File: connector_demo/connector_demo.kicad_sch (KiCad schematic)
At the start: 3 parts, among them J1 PicoBlade 8-wide, J2 PicoLock 8-wide, J3 MicroLock

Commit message: added connector names
still confirming pin 1
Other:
- company: (none) -> CalgaryToSpace
- title: (none) -> Connector PCB
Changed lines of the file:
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@@
 	(generator "eeschema")
 	(generator_version "9.0")
-	(paper "A4")
+	(paper "A")
+	(title_block
+		(title "Connector PCB")
+		(date "2025-03-28")
+		(rev "1")
+		(company "CalgaryToSpace")
+	)
 	(symbol
 		(lib_id "Connector_Generic:Conn_01x08")

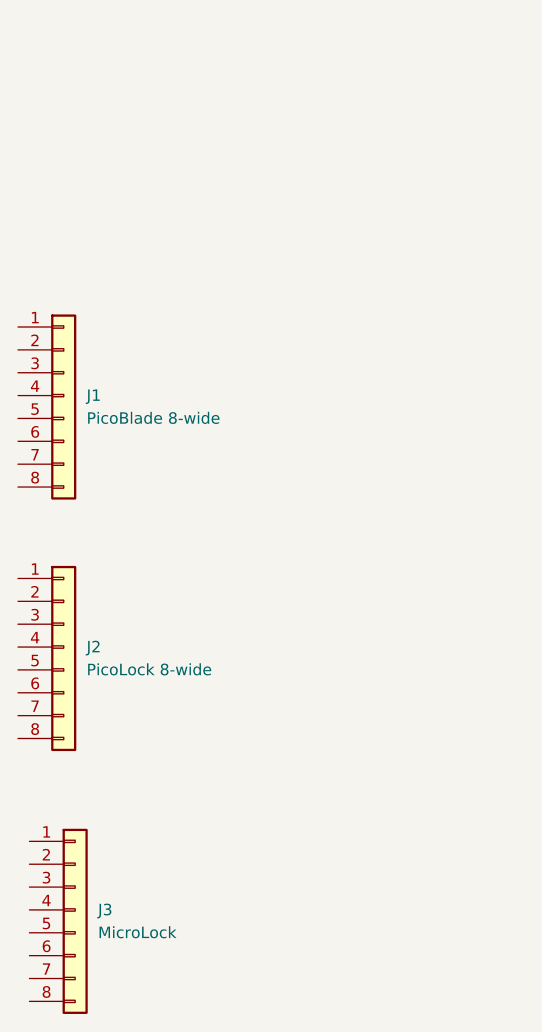
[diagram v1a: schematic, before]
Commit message: added header pins and traces
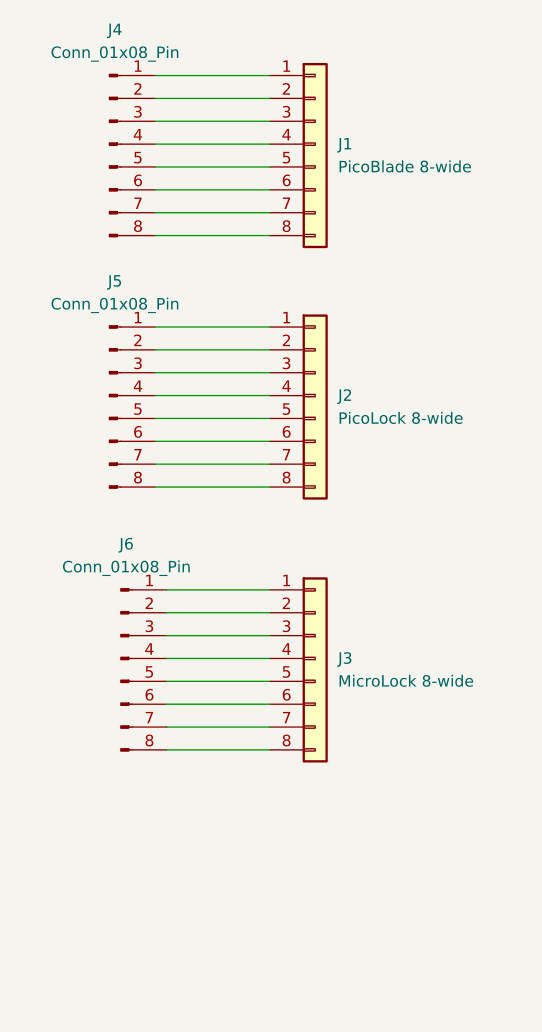
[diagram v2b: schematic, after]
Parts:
- added J4, J5, J6: Conn_01x08_Pin, Connector_PinHeader_2.54mm:PinHeader_1x08_P2.54mm_Vertical, symbol Connector:Conn_01x08_Pin
- J3: value MicroLock -> MicroLock 8-wide
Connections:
- net at J3.1 (Pin_1): now also J6.1 (Pin_1)
- net at J3.2 (Pin_2): now also J6.2 (Pin_2)
- net at J3.3 (Pin_3): now also J6.3 (Pin_3)
- net at J3.4 (Pin_4): now also J6.4 (Pin_4)
- net at J3.5 (Pin_5): now also J6.5 (Pin_5)
- net at J3.6 (Pin_6): now also J6.6 (Pin_6)
- net at J3.7 (Pin_7): now also J6.7 (Pin_7)
- net at J3.8 (Pin_8): now also J6.8 (Pin_8)
- net at J2.1 (Pin_1): now also J5.1 (Pin_1)
- net at J2.2 (Pin_2): now also J5.2 (Pin_2)
- net at J2.3 (Pin_3): now also J5.3 (Pin_3)
- net at J2.4 (Pin_4): now also J5.4 (Pin_4)
- net at J2.5 (Pin_5): now also J5.5 (Pin_5)
- net at J2.6 (Pin_6): now also J5.6 (Pin_6)
- net at J2.7 (Pin_7): now also J5.7 (Pin_7)
- net at J2.8 (Pin_8): now also J5.8 (Pin_8)
- net at J1.1 (Pin_1): now also J4.1 (Pin_1)
- net at J1.2 (Pin_2): now also J4.2 (Pin_2)
- net at J1.3 (Pin_3): now also J4.3 (Pin_3)
- net at J1.4 (Pin_4): now also J4.4 (Pin_4)
- net at J1.5 (Pin_5): now also J4.5 (Pin_5)
- net at J1.6 (Pin_6): now also J4.6 (Pin_6)
- net at J1.7 (Pin_7): now also J4.7 (Pin_7)
- net at J1.8 (Pin_8): now also J4.8 (Pin_8)
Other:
- moved on the sheet: J1, J2, J3

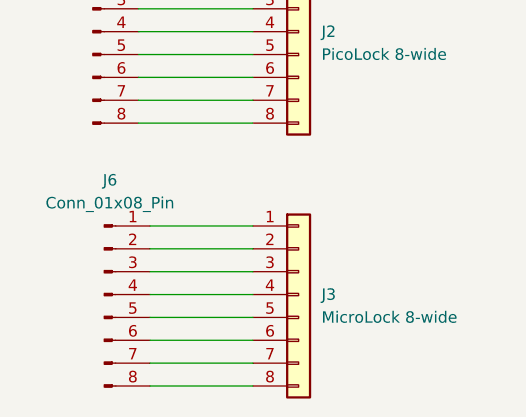
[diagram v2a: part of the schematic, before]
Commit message: Fixed microlock connector, generated BOM
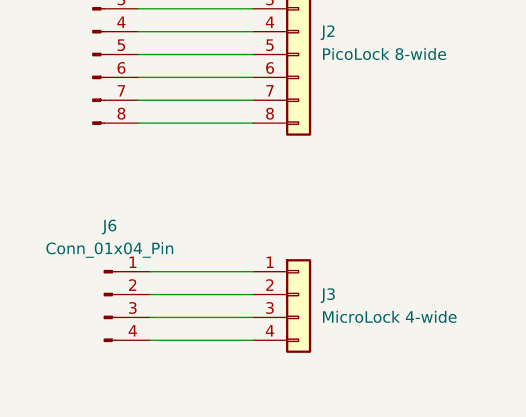
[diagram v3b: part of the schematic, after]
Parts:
- J3: value MicroLock 8-wide -> MicroLock 4-wide; footprint Connector_Molex:Molex_Pico-Lock_504050-0891_1x08-1MP_P1.50mm_Horizontal -> microlock:CONN04_5055670471_MOL; symbol Connector_Generic:Conn_01x08 -> Connector_Generic:Conn_01x04
- J6: value Conn_01x08_Pin -> Conn_01x04_Pin; footprint Connector_PinHeader_2.54mm:PinHeader_1x08_P2.54mm_Vertical -> Connector_PinHeader_2.54mm:PinHeader_1x04_P2.54mm_Vertical; symbol Connector:Conn_01x08_Pin -> Connector:Conn_01x04_Pin
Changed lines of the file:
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@@
-	(wire
-		(pts
-			(xy 87.63 111.76) (xy 99.06 111.76)
-		)
-		(stroke
-			(width 0)
-			(type default)
-		)
-	)
 	(wire
 		(pts
@@
 	(wire
 		(pts
-			(xy 87.63 99.06) (xy 99.06 99.06)
-		)
-		(stroke
-			(width 0)
-			(type default)
-		)
-	)
-	(wire
-		(pts
 			(xy 87.63 101.6) (xy 99.06 101.6)
 		)
@@
 	(wire
 		(pts
-			(xy 87.63 96.52) (xy 99.06 96.52)
-		)
-		(stroke
-			(width 0)
-			(type default)
-		)
-	)
-	(wire
-		(pts
 			(xy 86.36 46.99) (xy 99.06 46.99)
 		)
@@
 		(pts
 			(xy 86.36 82.55) (xy 99.06 82.55)
-		)
-		(stroke
-			(width 0)
-			(type default)
-		)
-	)
-	(wire
-		(pts
-			(xy 87.63 114.3) (xy 99.06 114.3)
 		)
 		(stroke
@@
 	)
 	(symbol
-		(lib_id "Connector_Generic:Conn_01x08")
+		(lib_id "Connector_Generic:Conn_01x04")
 		(at 104.14 104.14 0)
 		(unit 1)
@@
 			)
 		)
-		(property "Value" "MicroLock 8-wide"
+		(property "Value" "MicroLock 4-wide"
 			(at 106.68 106.6799 0)
 			(effects
@@
 			)
 		)
-		(property "Footprint" "Connector_Molex:Molex_Pico-Lock_504050-0891_1x08-1MP_P1.50mm_Horizontal"
+		(property "Footprint" "microlock:CONN04_5055670471_MOL"
 			(at 104.14 104.14 0)
 			(effects
@@
 			)
 		)
-		(property "Description" "Generic connector, single row, 01x08, script generated (kicad-library-utils/schlib/autogen/connector/)"
+		(property "Description" "Generic connector, single row, 01x04, script generated (kicad-library-utils/schlib/autogen/connector/)"
 			(at 104.14 104.14 0)
 			(effects
@@
 			)
 		)
-		(pin "6"
-		)
 		(pin "2"
 		)
-		(pin "5"
-		)
 		(pin "4"
 		)
@@
 		)
 		(pin "3"
-		)
-		(pin "8"
-		)
-		(pin "7"
 		)
 		(instances
@@
 	)
 	(symbol
-		(lib_id "Connector:Conn_01x08_Pin")
+		(lib_id "Connector:Conn_01x04_Pin")
 		(at 82.55 104.14 0)
 		(unit 1)
@@
 		(fields_autoplaced yes)
 		(property "Reference" "J6"
-			(at 83.185 91.44 0)
-			(effects
-				(font
-					(size 1.27 1.27)
-				)
-			)
-		)
-		(property "Value" "Conn_01x08_Pin"
-			(at 83.185 93.98 0)
-			(effects
-				(font
-					(size 1.27 1.27)
-				)
-			)
-		)
-		(property "Footprint" "Connector_PinHeader_2.54mm:PinHeader_1x08_P2.54mm_Vertical"
+			(at 83.185 96.52 0)
+			(effects
+				(font
+					(size 1.27 1.27)
+				)
+			)
+		)
+		(property "Value" "Conn_01x04_Pin"
+			(at 83.185 99.06 0)
+			(effects
+				(font
+					(size 1.27 1.27)
+				)
+			)
+		)
+		(property "Footprint" "Connector_PinHeader_2.54mm:PinHeader_1x04_P2.54mm_Vertical"
 			(at 82.55 104.14 0)
 			(effects
@@
 			)
 		)
-		(property "Description" "Generic connector, single row, 01x08, script generated"
+		(property "Description" "Generic connector, single row, 01x04, script generated"
 			(at 82.55 104.14 0)
 			(effects
@@
 			)
 		)
-		(pin "5"
-		)
-		(pin "6"
-		)
 		(pin "4"
 		)
 		(pin "3"
 		)
-		(pin "7"
-		)
-		(pin "8"
-		)
 		(pin "1"

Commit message: update microlock to 8 pin, confirmed pin 1
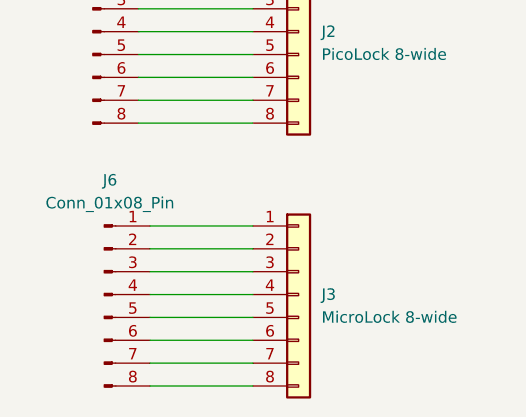
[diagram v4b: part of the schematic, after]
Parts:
- J3: value MicroLock 4-wide -> MicroLock 8-wide; footprint microlock:CONN04_5055670471_MOL -> microlock:CONN08_5055670871_MOL; symbol Connector_Generic:Conn_01x04 -> Connector_Generic:Conn_01x08
- J6: value Conn_01x04_Pin -> Conn_01x08_Pin; footprint Connector_PinHeader_2.54mm:PinHeader_1x04_P2.54mm_Vertical -> Connector_PinHeader_2.54mm:PinHeader_1x08_P2.54mm_Vertical; symbol Connector:Conn_01x04_Pin -> Connector:Conn_01x08_Pin
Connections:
- new net: J3.5 (Pin_5), J6.5 (Pin_5)
- new net: J3.6 (Pin_6), J6.6 (Pin_6)
- new net: J3.7 (Pin_7), J6.7 (Pin_7)
- new net: J3.8 (Pin_8), J6.8 (Pin_8)
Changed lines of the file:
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@@
+	(wire
+		(pts
+			(xy 87.63 114.3) (xy 99.06 114.3)
+		)
+		(stroke
+			(width 0)
+			(type default)
+		)
+	)
 	(wire
 		(pts
@@
 	(wire
 		(pts
+			(xy 87.63 111.76) (xy 99.06 111.76)
+		)
+		(stroke
+			(width 0)
+			(type default)
+		)
+	)
+	(wire
+		(pts
 			(xy 86.36 67.31) (xy 99.06 67.31)
 		)
@@
 	(wire
 		(pts
+			(xy 87.63 99.06) (xy 99.06 99.06)
+		)
+		(stroke
+			(width 0)
+			(type default)
+		)
+	)
+	(wire
+		(pts
 			(xy 86.36 80.01) (xy 99.06 80.01)
 		)
@@
 		(pts
 			(xy 86.36 49.53) (xy 99.06 49.53)
+		)
+		(stroke
+			(width 0)
+			(type default)
+		)
+	)
+	(wire
+		(pts
+			(xy 87.63 96.52) (xy 99.06 96.52)
 		)
 		(stroke
@@
 	)
 	(symbol
-		(lib_id "Connector_Generic:Conn_01x04")
+		(lib_id "Connector_Generic:Conn_01x08")
 		(at 104.14 104.14 0)
 		(unit 1)
@@
 			)
 		)
-		(property "Value" "MicroLock 4-wide"
+		(property "Value" "MicroLock 8-wide"
 			(at 106.68 106.6799 0)
 			(effects
@@
 			)
 		)
-		(property "Footprint" "microlock:CONN04_5055670471_MOL"
+		(property "Footprint" "microlock:CONN08_5055670871_MOL"
 			(at 104.14 104.14 0)
 			(effects
@@
 			)
 		)
-		(property "Description" "Generic connector, single row, 01x04, script generated (kicad-library-utils/schlib/autogen/connector/)"
+		(property "Description" "Generic connector, single row, 01x08, script generated (kicad-library-utils/schlib/autogen/connector/)"
 			(at 104.14 104.14 0)
 			(effects
@@
 		)
 		(pin "3"
+		)
+		(pin "8"
+		)
+		(pin "5"
+		)
+		(pin "6"
+		)
+		(pin "7"
 		)
 		(instances
@@
 	)
 	(symbol
-		(lib_id "Connector:Conn_01x04_Pin")
+		(lib_id "Connector:Conn_01x08_Pin")
 		(at 82.55 104.14 0)
 		(unit 1)
@@
 		(fields_autoplaced yes)
 		(property "Reference" "J6"
-			(at 83.185 96.52 0)
-			(effects
-				(font
-					(size 1.27 1.27)
-				)
-			)
-		)
-		(property "Value" "Conn_01x04_Pin"
-			(at 83.185 99.06 0)
-			(effects
-				(font
-					(size 1.27 1.27)
-				)
-			)
-		)
-		(property "Footprint" "Connector_PinHeader_2.54mm:PinHeader_1x04_P2.54mm_Vertical"
+			(at 83.185 91.44 0)
+			(effects
+				(font
+					(size 1.27 1.27)
+				)
+			)
+		)
+		(property "Value" "Conn_01x08_Pin"
+			(at 83.185 93.98 0)
+			(effects
+				(font
+					(size 1.27 1.27)
+				)
+			)
+		)
+		(property "Footprint" "Connector_PinHeader_2.54mm:PinHeader_1x08_P2.54mm_Vertical"
 			(at 82.55 104.14 0)
 			(effects
@@
 			)
 		)
-		(property "Description" "Generic connector, single row, 01x04, script generated"
+		(property "Description" "Generic connector, single row, 01x08, script generated"
 			(at 82.55 104.14 0)
 			(effects
@@
 		(pin "2"
 		)
+		(pin "5"
+		)
+		(pin "7"
+		)
+		(pin "8"
+		)
+		(pin "6"
+		)
 		(instances
